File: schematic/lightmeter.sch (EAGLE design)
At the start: 69 parts, among them J1 CONNECTEDJUMPER, J2 CONNECTEDJUMPER, Q1 NCHANNELMOSFET, Q2 NCHANNELMOSFET, Q3 PCHANNELMOSFET

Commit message: Some more work on board layout.
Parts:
- renumbered R300 to R3, R400 to R4
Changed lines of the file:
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@@
 <part name="C12" library="rcl" deviceset="C-EU" device="C0402" value="u1"/>
 <part name="GND16" library="supply1" deviceset="GND" device=""/>
-<part name="R400" library="resistor" deviceset="R-EU_" device="R0402" value="1k"/>
-<part name="R300" library="resistor" deviceset="R-EU_" device="R0402" value="1k"/>
+<part name="R4" library="resistor" deviceset="R-EU_" device="R0402" value="1k"/>
+<part name="R3" library="resistor" deviceset="R-EU_" device="R0402" value="1k"/>
 <part name="C14" library="rcl" deviceset="C-EU" device="C0402" value="u1"/>
 <part name="U1" library="lightmeter" deviceset="USB-AB" device="USB-AB-MICRO-MIDMOUNT"/>
@@
 <instance part="C12" gate="G$1" x="-17.78" y="53.34" rot="R90"/>
 <instance part="GND16" gate="1" x="-25.4" y="53.34" rot="R270"/>
-<instance part="R400" gate="G$1" x="25.4" y="58.42" rot="R90"/>
-<instance part="R300" gate="G$1" x="25.4" y="68.58" rot="R180"/>
+<instance part="R4" gate="G$1" x="25.4" y="58.42" rot="R90"/>
+<instance part="R3" gate="G$1" x="25.4" y="68.58" rot="R180"/>
 <instance part="C14" gate="G$1" x="30.48" y="53.34"/>
 <instance part="U1" gate="G$1" x="-83.82" y="88.9"/>
@@
 </segment>
 <segment>
-<pinref part="R400" gate="G$1" pin="1"/>
+<pinref part="R4" gate="G$1" pin="1"/>
 <wire x1="25.4" y1="53.34" x2="22.86" y2="53.34" width="0.1524" layer="91"/>
 <wire x1="22.86" y1="53.34" x2="22.86" y2="58.42" width="0.1524" layer="91"/>
 <pinref part="IC$6" gate="G$1" pin="VDDIO"/>
 <wire x1="22.86" y1="58.42" x2="17.78" y2="58.42" width="0.1524" layer="91"/>
-<pinref part="R300" gate="G$1" pin="1"/>
+<pinref part="R3" gate="G$1" pin="1"/>
 <wire x1="30.48" y1="68.58" x2="30.48" y2="58.42" width="0.1524" layer="91"/>
 <wire x1="30.48" y1="58.42" x2="22.86" y2="58.42" width="0.1524" layer="91"/>
@@
 <segment>
 <pinref part="IC$6" gate="G$1" pin="SDA"/>
-<pinref part="R300" gate="G$1" pin="2"/>
+<pinref part="R3" gate="G$1" pin="2"/>
 <wire x1="17.78" y1="68.58" x2="20.32" y2="68.58" width="0.1524" layer="91"/>
 <wire x1="20.32" y1="68.58" x2="20.32" y2="76.2" width="0.1524" layer="91"/>
@@
 <wire x1="-10.16" y1="63.5" x2="-10.16" y2="66.04" width="0.1524" layer="91"/>
 <wire x1="-10.16" y1="66.04" x2="25.4" y2="66.04" width="0.1524" layer="91"/>
-<pinref part="R400" gate="G$1" pin="2"/>
+<pinref part="R4" gate="G$1" pin="2"/>
 <wire x1="25.4" y1="66.04" x2="25.4" y2="63.5" width="0.1524" layer="91"/>
 <wire x1="-10.16" y1="63.5" x2="-12.7" y2="63.5" width="0.1524" layer="91"/>

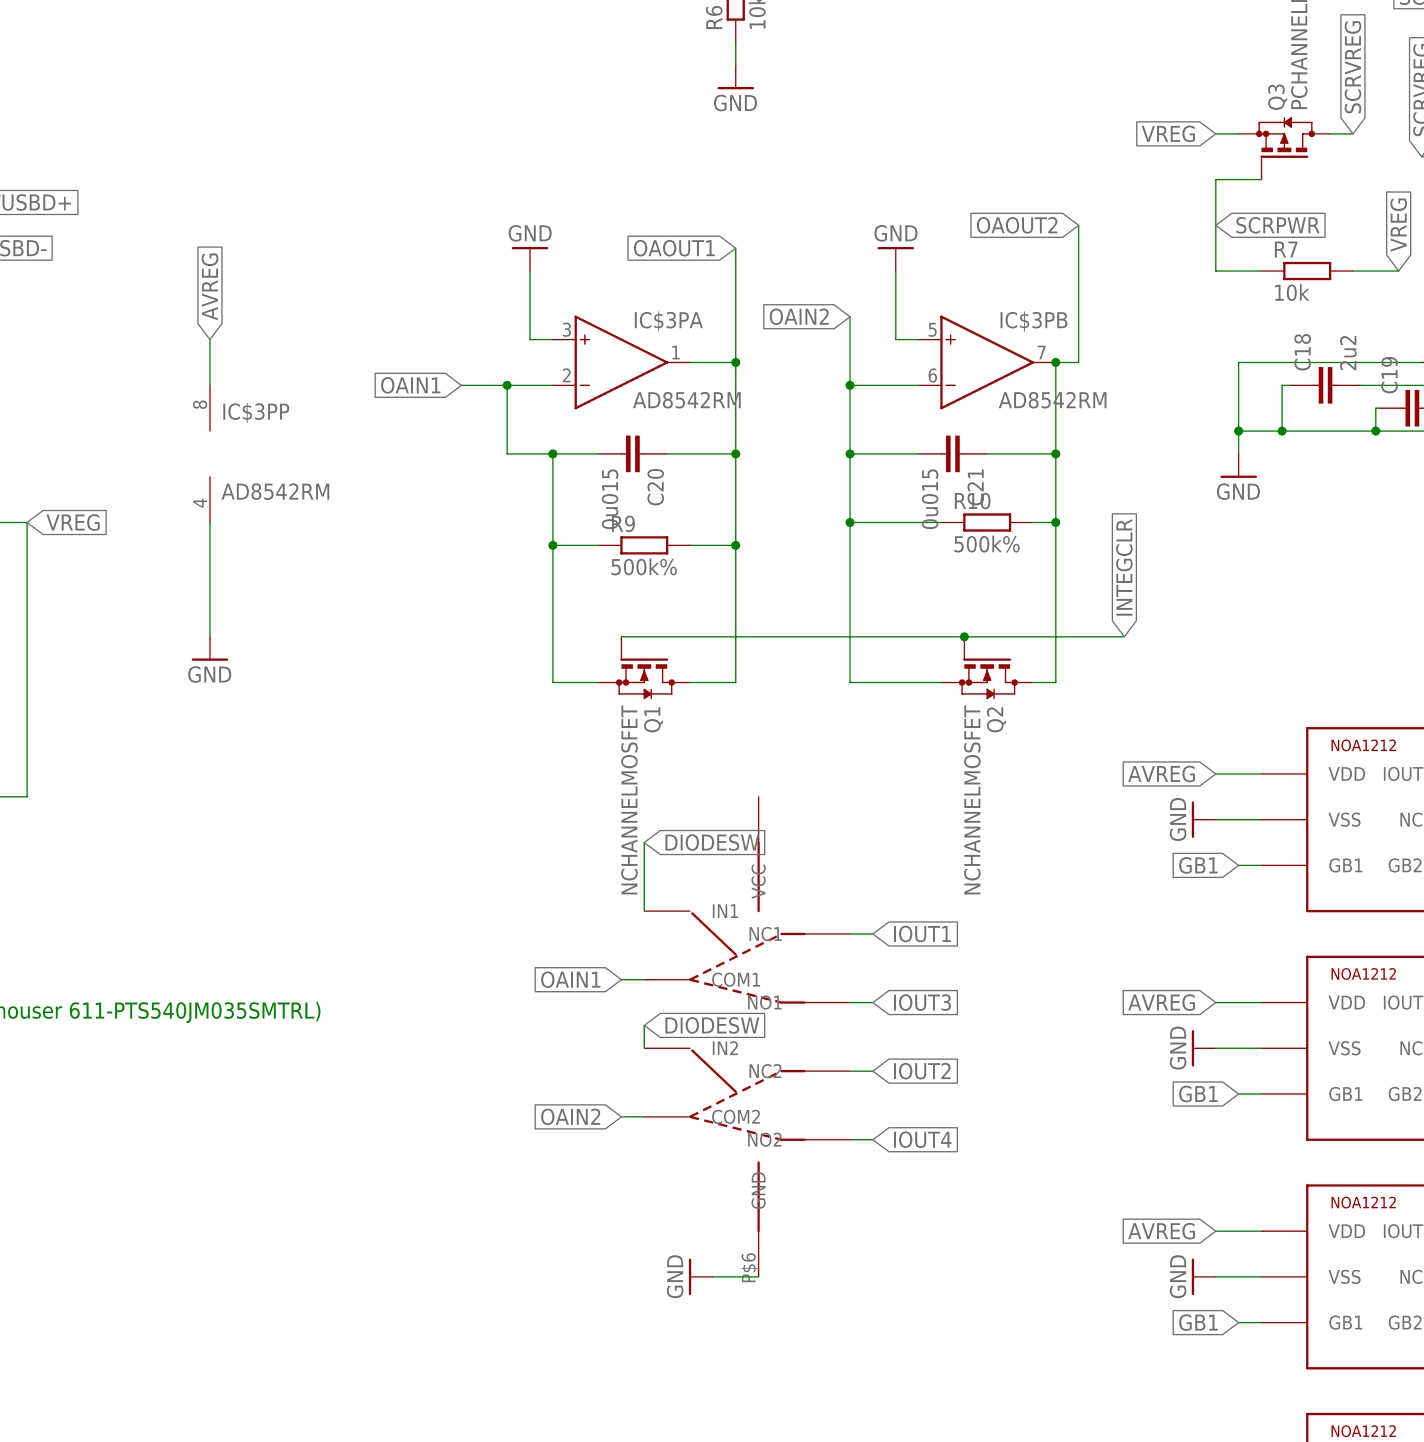
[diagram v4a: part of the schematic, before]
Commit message: More work on board layout.
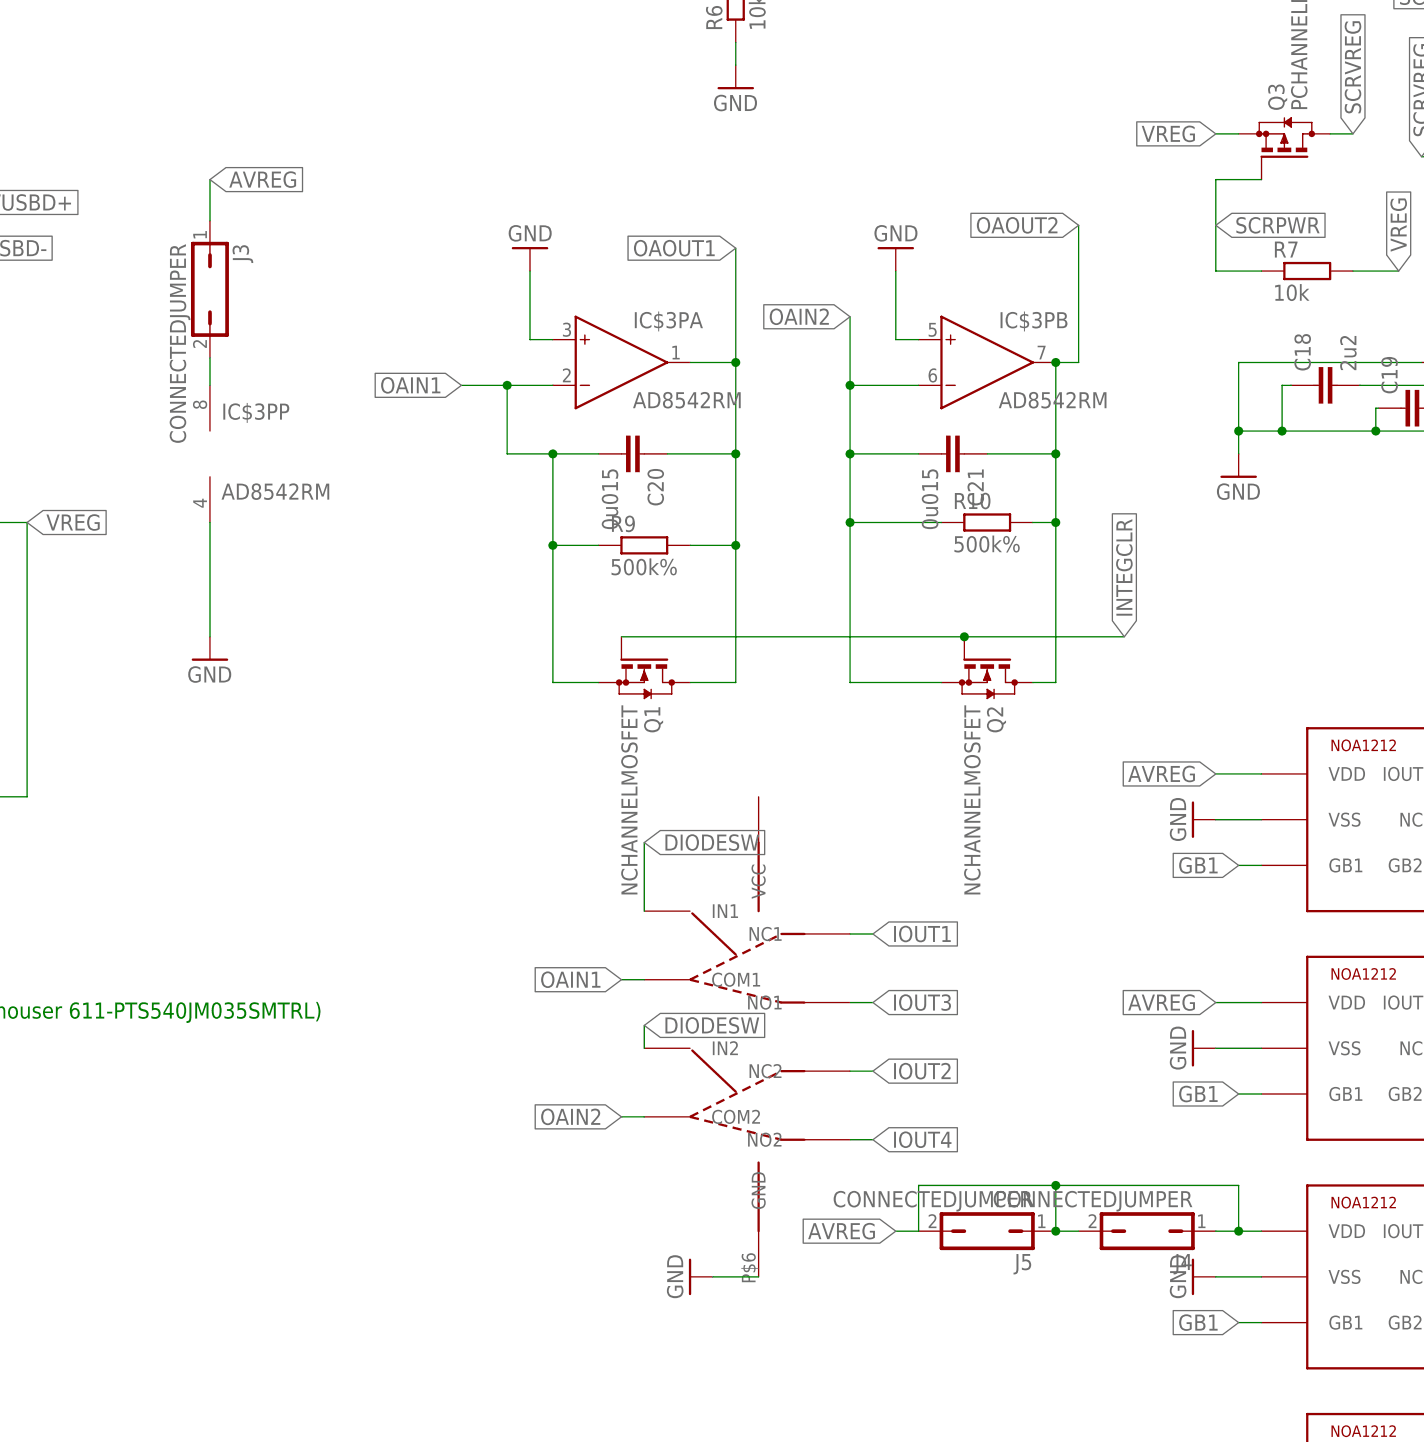
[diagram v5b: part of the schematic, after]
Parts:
- added J3, J4, J5: CONNECTEDJUMPER, lightmeter:CONNECTEDJUMPER
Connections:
- new net N$3: IC$3PP.V+, J3.2
- net AVREG: now also J3.1, J4.1, J4.2, J5.1, J5.2; no longer IC$3PP.V+
- net GB1: now also IC$9.GB1
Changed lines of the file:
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@@
 <part name="J2" library="lightmeter" deviceset="CONNECTEDJUMPER" device=""/>
 <part name="H1" library="pinhead" deviceset="PINHD-1X1" device=""/>
+<part name="J3" library="lightmeter" deviceset="CONNECTEDJUMPER" device=""/>
+<part name="J4" library="lightmeter" deviceset="CONNECTEDJUMPER" device=""/>
+<part name="J5" library="lightmeter" deviceset="CONNECTEDJUMPER" device=""/>
 </parts>
 <sheets>
@@
 <instance part="J2" gate="G$1" x="190.5" y="-132.08"/>
 <instance part="H1" gate="G$1" x="-63.5" y="48.26"/>
+<instance part="J3" gate="G$1" x="38.1" y="-2.032" rot="R90"/>
+<instance part="J4" gate="G$1" x="142.24" y="-106.68"/>
+<instance part="J5" gate="G$1" x="124.46" y="-106.68"/>
 </instances>
 <busses>
@@
 </segment>
 <segment>
-<pinref part="IC$3P" gate="P" pin="V+"/>
-<wire x1="38.1" y1="-12.7" x2="38.1" y2="-7.62" width="0.1524" layer="91"/>
-<label x="38.1" y="-7.62" size="1.778" layer="95" rot="R90" xref="yes"/>
-</segment>
-<segment>
 <pinref part="IC$3" gate="G$1" pin="OUT"/>
 <wire x1="-78.74" y1="-71.12" x2="-76.2" y2="-71.12" width="0.1524" layer="91"/>
@@
 </segment>
 <segment>
-<pinref part="IC$9" gate="G$1" pin="VDD"/>
-<wire x1="154.94" y1="-106.68" x2="149.86" y2="-106.68" width="0.1524" layer="91"/>
-<label x="149.86" y="-106.68" size="1.778" layer="95" rot="R180" xref="yes"/>
-</segment>
-<segment>
 <pinref part="IC$10" gate="G$1" pin="VDD"/>
 <wire x1="154.94" y1="-132.08" x2="149.86" y2="-132.08" width="0.1524" layer="91"/>
 <label x="149.86" y="-132.08" size="1.778" layer="95" rot="R180" xref="yes"/>
+</segment>
+<segment>
+<pinref part="J3" gate="G$1" pin="1"/>
+<wire x1="38.1" y1="5.588" x2="38.1" y2="10.16" width="0.1524" layer="91"/>
+<label x="38.1" y="10.16" size="1.778" layer="95" xref="yes"/>
+</segment>
+<segment>
+<pinref part="J5" gate="G$1" pin="2"/>
+<label x="114.3" y="-106.68" size="1.778" layer="95" rot="R180" xref="yes"/>
+<wire x1="114.3" y1="-106.68" x2="116.84" y2="-106.68" width="0.1524" layer="91"/>
+<wire x1="116.84" y1="-106.68" x2="116.84" y2="-101.6" width="0.1524" layer="91"/>
+<wire x1="116.84" y1="-101.6" x2="132.08" y2="-101.6" width="0.1524" layer="91"/>
+<pinref part="J4" gate="G$1" pin="2"/>
+<pinref part="J5" gate="G$1" pin="1"/>
+<wire x1="134.62" y1="-106.68" x2="132.08" y2="-106.68" width="0.1524" layer="91"/>
+<wire x1="132.08" y1="-101.6" x2="132.08" y2="-106.68" width="0.1524" layer="91"/>
+<junction x="132.08" y="-106.68"/>
+<wire x1="132.08" y1="-101.6" x2="152.4" y2="-101.6" width="0.1524" layer="91"/>
+<junction x="132.08" y="-101.6"/>
+<pinref part="IC$9" gate="G$1" pin="VDD"/>
+<pinref part="J4" gate="G$1" pin="1"/>
+<wire x1="154.94" y1="-106.68" x2="152.4" y2="-106.68" width="0.1524" layer="91"/>
+<wire x1="152.4" y1="-106.68" x2="149.86" y2="-106.68" width="0.1524" layer="91"/>
+<wire x1="152.4" y1="-101.6" x2="152.4" y2="-106.68" width="0.1524" layer="91"/>
+<junction x="152.4" y="-106.68"/>
 </segment>
 </net>
@@
 <wire x1="154.94" y1="-116.84" x2="152.4" y2="-116.84" width="0.1524" layer="91"/>
 <label x="152.4" y="-116.84" size="1.778" layer="95" rot="R180" xref="yes"/>
+<pinref part="IC$9" gate="G$1" pin="GB1"/>
 </segment>
 <segment>
@@
 </segment>
 </net>
+<net name="N$3" class="0">
+<segment>
+<pinref part="IC$3P" gate="P" pin="V+"/>
+<wire x1="38.1" y1="-12.7" x2="38.1" y2="-9.652" width="0.1524" layer="91"/>
+<pinref part="J3" gate="G$1" pin="2"/>
+</segment>
+</net>

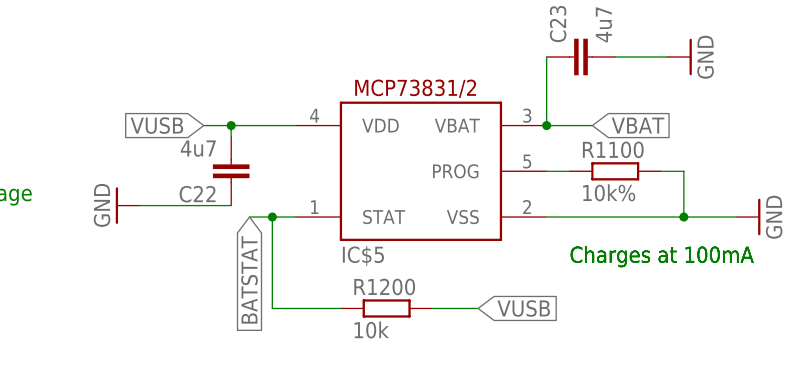
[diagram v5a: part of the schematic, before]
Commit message: More work on board layout.
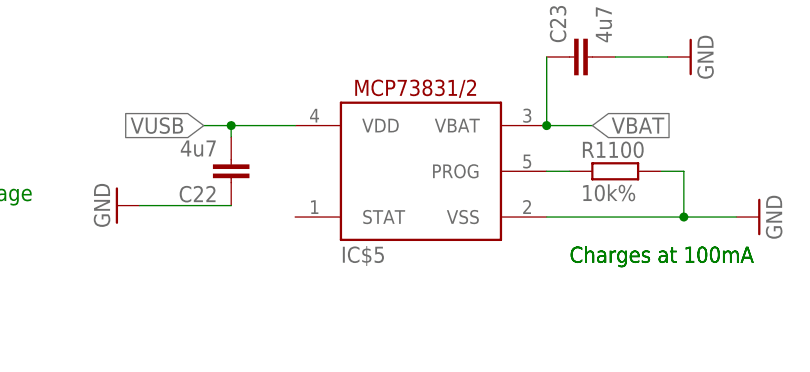
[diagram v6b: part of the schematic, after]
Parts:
- removed R1200: 10k, resistor:R-EU_R0402
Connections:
- removed net BATSTAT: IC$5.STAT, R1200.1
- net VUSB: no longer R1200.2
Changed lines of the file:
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@@
 <part name="IC$5" library="adafruit" deviceset="MCP73831" device="/OT"/>
 <part name="GND6" library="supply1" deviceset="GND" device=""/>
-<part name="R1200" library="resistor" deviceset="R-EU_" device="R0402" value="10k"/>
 <part name="R1100" library="resistor" deviceset="R-EU_" device="R0402" value="10k%"/>
 <part name="GND26" library="supply1" deviceset="GND" device=""/>
@@
 <instance part="IC$5" gate="G$1" x="-19.558" y="-131.318"/>
 <instance part="GND6" gate="1" x="19.304" y="-136.398" rot="R90"/>
-<instance part="R1200" gate="G$1" x="-22.098" y="-146.558"/>
 <instance part="R1100" gate="G$1" x="3.302" y="-131.318"/>
 <instance part="GND26" gate="1" x="-148.844" y="-12.7" rot="R270"/>
@@
 </segment>
 <segment>
-<pinref part="R1200" gate="G$1" pin="2"/>
-<wire x1="-17.018" y1="-146.558" x2="-11.938" y2="-146.558" width="0.1524" layer="91"/>
-<label x="-11.938" y="-146.558" size="1.778" layer="95" xref="yes"/>
-</segment>
-<segment>
 <label x="-96.52" y="83.82" size="1.778" layer="95" rot="R270" xref="yes"/>
 <pinref part="U1" gate="G$1" pin="VBUS"/>
@@
 </segment>
 </net>
-<net name="BATSTAT" class="0">
-<segment>
-<pinref part="IC$5" gate="G$1" pin="STAT"/>
-<wire x1="-32.258" y1="-136.398" x2="-34.798" y2="-136.398" width="0.1524" layer="91"/>
-<label x="-37.338" y="-136.398" size="1.778" layer="95" rot="R270" xref="yes"/>
-<wire x1="-34.798" y1="-136.398" x2="-37.338" y2="-136.398" width="0.1524" layer="91"/>
-<wire x1="-34.798" y1="-136.398" x2="-34.798" y2="-146.558" width="0.1524" layer="91"/>
-<junction x="-34.798" y="-136.398"/>
-<pinref part="R1200" gate="G$1" pin="1"/>
-<wire x1="-27.178" y1="-146.558" x2="-34.798" y2="-146.558" width="0.1524" layer="91"/>
-</segment>
-</net>

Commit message: More work on layout.
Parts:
- removed R6: 10k, resistor:R-EU_R0402
- added J6: CONNECTEDJUMPER, lightmeter:CONNECTEDJUMPER
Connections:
- removed net N$13: D3.A, R6.2
- new net N$4: IC$2.EN, IC$2.VIN, J6.1
- net GND: now also D3.A; no longer R6.1
- net VCC: now also J6.2; no longer IC$2.EN, IC$2.VIN
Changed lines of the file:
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@@
 <part name="D3" library="lightmeter" deviceset="GSOT04-E3-08" device=""/>
 <part name="GND32" library="supply1" deviceset="GND" device=""/>
-<part name="R6" library="resistor" deviceset="R-EU_" device="R0402" value="10k"/>
 <part name="IC$7" library="lightmeter" deviceset="NOA1212" device=""/>
 <part name="IC$8" library="lightmeter" deviceset="NOA1212" device=""/>
@@
 <part name="J4" library="lightmeter" deviceset="CONNECTEDJUMPER" device=""/>
 <part name="J5" library="lightmeter" deviceset="CONNECTEDJUMPER" device=""/>
+<part name="J6" library="lightmeter" deviceset="CONNECTEDJUMPER" device=""/>
 </parts>
 <sheets>
@@
 <plain>
 <text x="-152.4" y="-7.62" size="1.778" layer="91">Battery (3.7V nominal)</text>
-<text x="-55.88" y="101.6" size="1.778" layer="91">Buck regulator LM3671 (outputs 2.8 volts)</text>
+<text x="-40.64" y="101.6" size="1.778" layer="91">Buck regulator LM3671 (outputs 2.8 volts)</text>
 <text x="-1.778" y="-83.058" size="1.778" layer="91">Pushbuttons (mouser 611-PTS540JM035SMTRL)</text>
 <text x="213.36" y="60.96" size="1.778" layer="91">Screen (C2P right, IREF left)</text>
@@
 <instance part="D3" gate="G$1" x="96.52" y="40.64" rot="R90"/>
 <instance part="GND32" gate="1" x="96.52" y="20.32"/>
-<instance part="R6" gate="G$1" x="96.52" y="30.48" rot="R90"/>
 <instance part="IC$7" gate="G$1" x="167.64" y="-60.96"/>
 <instance part="IC$8" gate="G$1" x="167.64" y="-86.36"/>
@@
 <instance part="J4" gate="G$1" x="142.24" y="-106.68"/>
 <instance part="J5" gate="G$1" x="124.46" y="-106.68"/>
+<instance part="J6" gate="G$1" x="-53.34" y="101.6"/>
 </instances>
 <busses>
@@
 </segment>
 <segment>
-<pinref part="R6" gate="G$1" pin="1"/>
 <pinref part="GND32" gate="1" pin="GND"/>
-<wire x1="96.52" y1="25.4" x2="96.52" y2="22.86" width="0.1524" layer="91"/>
+<pinref part="D3" gate="G$1" pin="A"/>
+<wire x1="96.52" y1="38.1" x2="96.52" y2="22.86" width="0.1524" layer="91"/>
 </segment>
 <segment>
@@
 <net name="VCC" class="0">
 <segment>
+<pinref part="J6" gate="G$1" pin="2"/>
+<wire x1="-63.5" y1="101.6" x2="-60.96" y2="101.6" width="0.1524" layer="91"/>
+<wire x1="-63.5" y1="99.06" x2="-63.5" y2="101.6" width="0.1524" layer="91"/>
+<wire x1="-58.42" y1="99.06" x2="-63.5" y2="99.06" width="0.1524" layer="91"/>
 <pinref part="P+3" gate="VCC" pin="VCC"/>
-<wire x1="-41.402" y1="93.98" x2="-45.72" y2="93.98" width="0.1524" layer="91"/>
-<wire x1="-45.72" y1="93.98" x2="-58.42" y2="93.98" width="0.1524" layer="91"/>
 <wire x1="-58.42" y1="93.98" x2="-60.96" y2="93.98" width="0.1524" layer="91"/>
+<wire x1="-58.42" y1="93.98" x2="-58.42" y2="99.06" width="0.1524" layer="91"/>
+<junction x="-58.42" y="93.98"/>
+<pinref part="C9" gate="G$1" pin="2"/>
 <wire x1="-55.88" y1="88.9" x2="-58.42" y2="88.9" width="0.1524" layer="91"/>
 <wire x1="-58.42" y1="88.9" x2="-58.42" y2="93.98" width="0.1524" layer="91"/>
-<junction x="-58.42" y="93.98"/>
-<wire x1="-41.402" y1="83.82" x2="-45.72" y2="83.82" width="0.1524" layer="91"/>
-<wire x1="-45.72" y1="83.82" x2="-45.72" y2="93.98" width="0.1524" layer="91"/>
-<junction x="-45.72" y="93.98"/>
-<pinref part="IC$2" gate="G$1" pin="VIN"/>
-<pinref part="IC$2" gate="G$1" pin="EN"/>
-<pinref part="C9" gate="G$1" pin="2"/>
 </segment>
 <segment>
@@
 </segment>
 </net>
-<net name="N$13" class="0">
-<segment>
-<pinref part="R6" gate="G$1" pin="2"/>
-<pinref part="D3" gate="G$1" pin="A"/>
-<wire x1="96.52" y1="35.56" x2="96.52" y2="38.1" width="0.1524" layer="91"/>
-</segment>
-</net>
 <net name="GB2" class="0">
 <segment>
@@
 </segment>
 </net>
+<net name="N$4" class="0">
+<segment>
+<wire x1="-41.402" y1="93.98" x2="-45.72" y2="93.98" width="0.1524" layer="91"/>
+<wire x1="-41.402" y1="83.82" x2="-45.72" y2="83.82" width="0.1524" layer="91"/>
+<wire x1="-45.72" y1="83.82" x2="-45.72" y2="93.98" width="0.1524" layer="91"/>
+<pinref part="IC$2" gate="G$1" pin="VIN"/>
+<pinref part="IC$2" gate="G$1" pin="EN"/>
+<pinref part="J6" gate="G$1" pin="1"/>
+<wire x1="-45.72" y1="93.98" x2="-45.72" y2="101.6" width="0.1524" layer="91"/>
+<junction x="-45.72" y="93.98"/>
+</segment>
+</net>
